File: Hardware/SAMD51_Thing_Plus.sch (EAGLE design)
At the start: 48 parts, among them J6 AMP FCI 10103594-0001LF, Q1 2.5A/30V, U1 MCP73831, U2 ATSAMD51J20A-A, U3 AP2112K-3.3V, U4 4MB Flash, Y1 32.768kHz

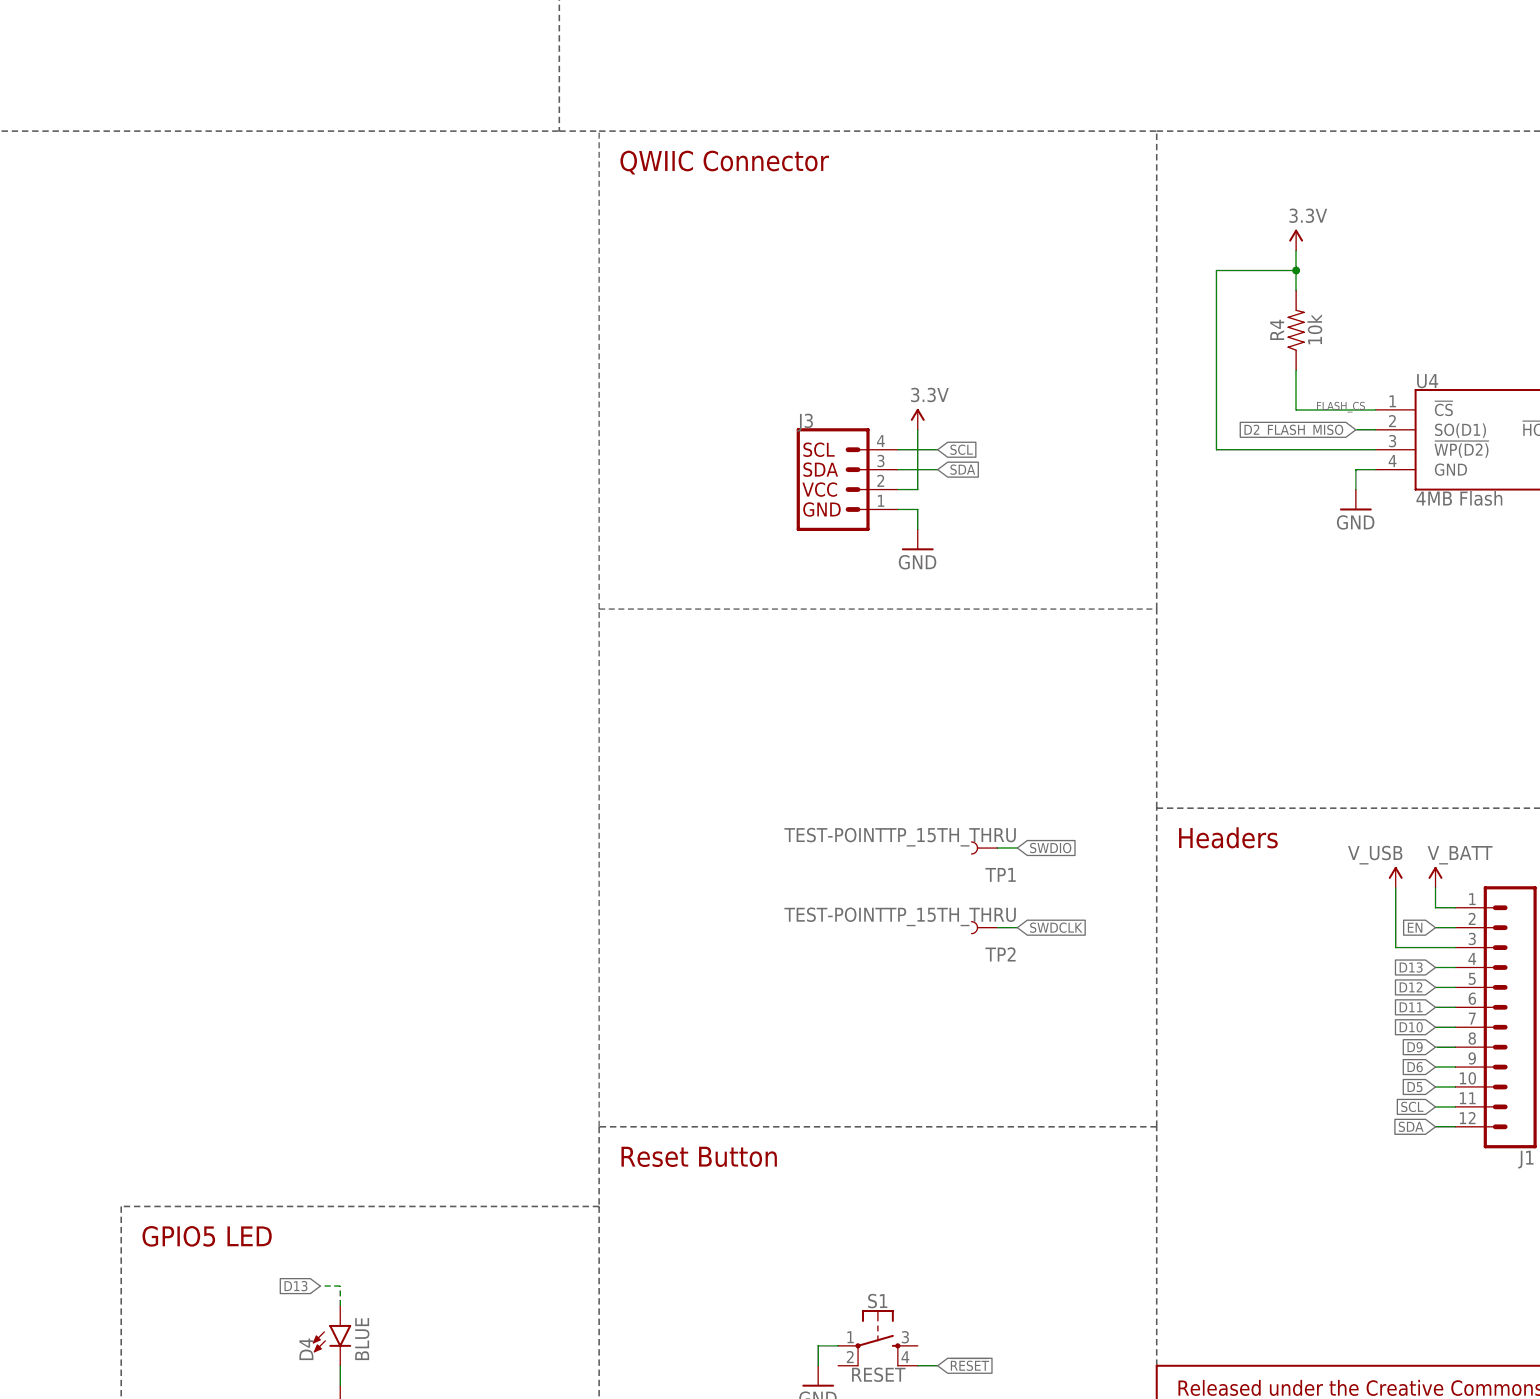
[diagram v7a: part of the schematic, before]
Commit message: A few more changes to text labels on schematic
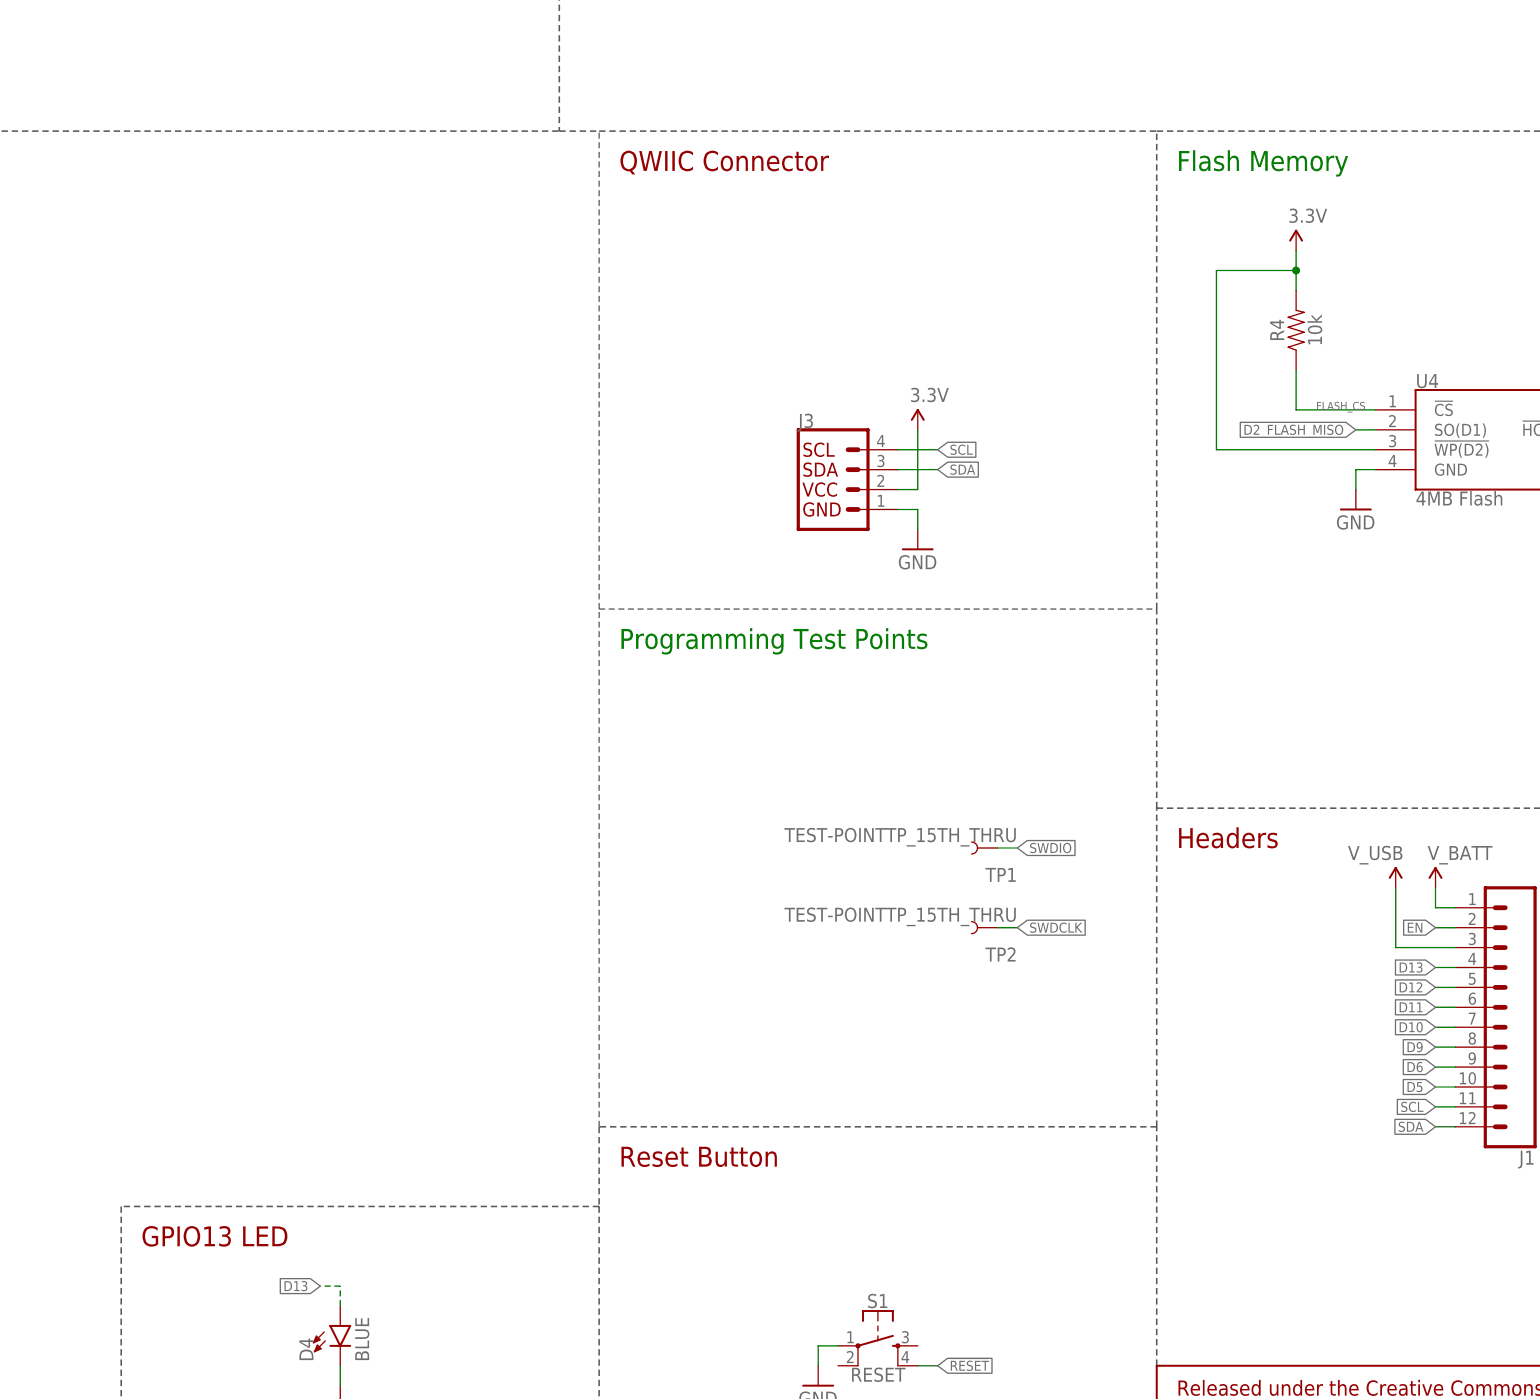
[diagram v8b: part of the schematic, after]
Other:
- note added: "Flash Memory"
- note added: "GPIO13 LED"
- note added: "Programming Test Points"
- note removed: "GPIO5 LED"
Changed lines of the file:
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@@
 <wire x1="259.08" y1="55.88" x2="198.12" y2="55.88" width="0.2032" layer="97" style="longdash"/>
 <text x="261.62" y="63.5" size="2.54" layer="94" font="vector" align="top-left">Reset Button</text>
-<text x="200.66" y="53.34" size="2.54" layer="94" font="vector" align="top-left">GPIO5 LED</text>
-<text x="332.74" y="104.14" size="2.54" layer="94" align="top-left">Headers</text>
+<text x="200.66" y="53.34" size="2.54" layer="94" font="vector" align="top-left">GPIO13 LED</text>
+<text x="332.74" y="104.14" size="2.54" layer="94" font="vector" align="top-left">Headers</text>
 <text x="421.64" y="10.16" size="2.54" layer="94" font="vector" align="top-left">01</text>
 <text x="69.088" y="17.78" size="0.4064" layer="94">C8 to be
@@
 <wire x1="259.08" y1="132.08" x2="330.2" y2="132.08" width="0.1524" layer="97" style="longdash"/>
 <text x="350.52" y="7.62" size="3.81" layer="94" font="vector">Mike Hord</text>
+<text x="261.62" y="127" size="2.54" layer="91" font="vector">Programming Test Points</text>
+<text x="332.74" y="187.96" size="2.54" layer="91" font="vector">Flash Memory</text>
 </plain>
 <instances>
